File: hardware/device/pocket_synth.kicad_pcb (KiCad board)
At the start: 4 copper layers, 72 x 150 mm, 98 parts, among them J10 MIDI_OUT, J2 USB, J3 Micro_SD_Card_Det_Hirose_DM3AT, J6 LINE_IN, J8 LINE_OUT, J9 MIDI_IN, SW1 TRIG1, SW10 TRIG10, SW11 TRIG11, SW12 TRIG12, SW13 TRIG13, SW14 TRIG14, SW15 TRIG15, SW16 TRIG16, SW2 TRIG2, SW3 TRIG3, SW4 TRIG4, SW5 TRIG5, SW6 TRIG6, SW7 TRIG7, SW8 TRIG8, SW9 TRIG9, U1 VOL_PWR_POT, U10 TRIG9, U11 TRIG13, U12 TRIG10, U13 TRIG14, U14 TRIG11, U15 TRIG15, U16 TRIG12, U17 TRIG16, U18 STM32H743ZIT6, U2 TRIG1, U20 TPS62A02DRL, U21 TPS560200, U22 MAX17261xxTD, U23 BQ21040DBV, U25 TCA8418RTWR, U26 FUSB303BTMX, U27 FUSB302B01MPX, U3 TRIG2, U4 TRIG3, U5 TRIG4, U6 TRIG8, U7 TRIG7, U8 TRIG6, U9 TRIG5

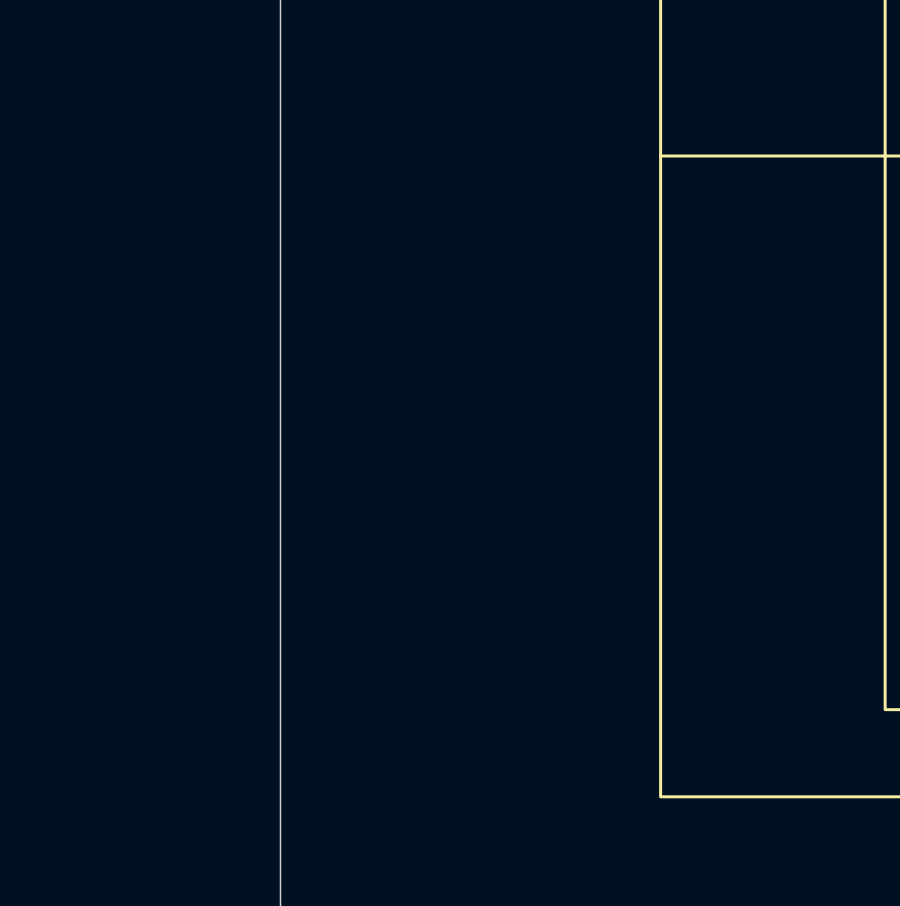
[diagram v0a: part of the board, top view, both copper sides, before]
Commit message: feat: project organization, add knob, pcb layout, and 3d models
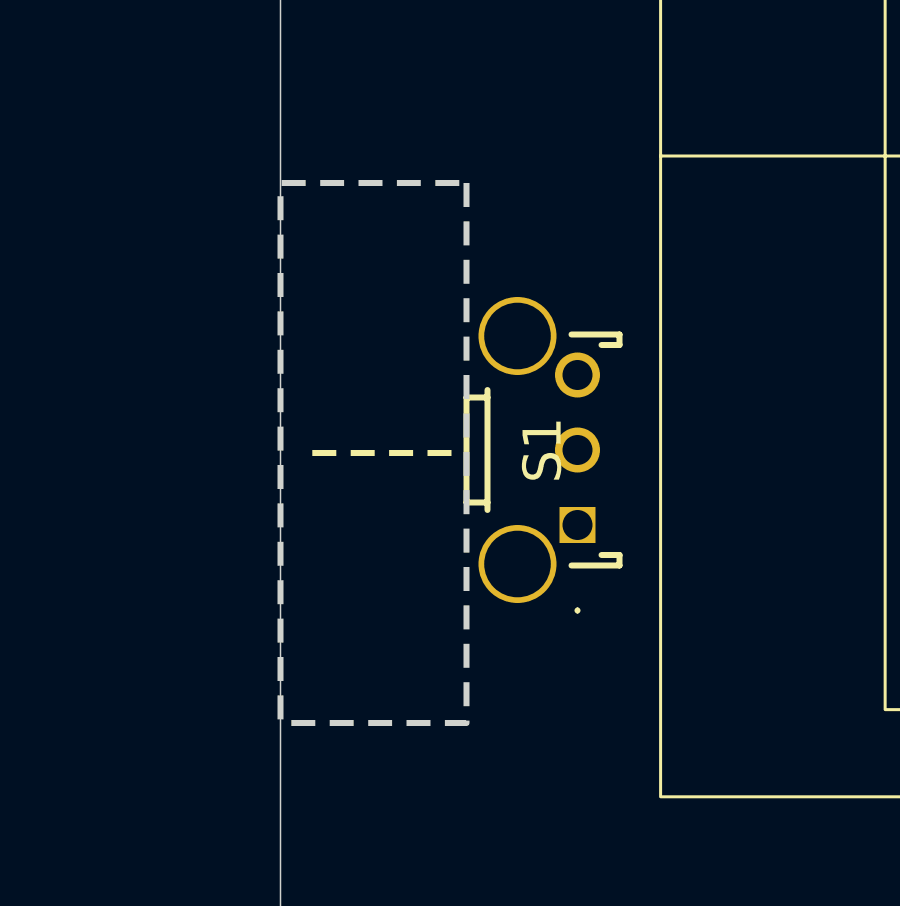
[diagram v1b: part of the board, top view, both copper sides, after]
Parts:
- added S1: ENCODER, pocket_synth:2416191-1, F.Cu at (46.7, 81.2)

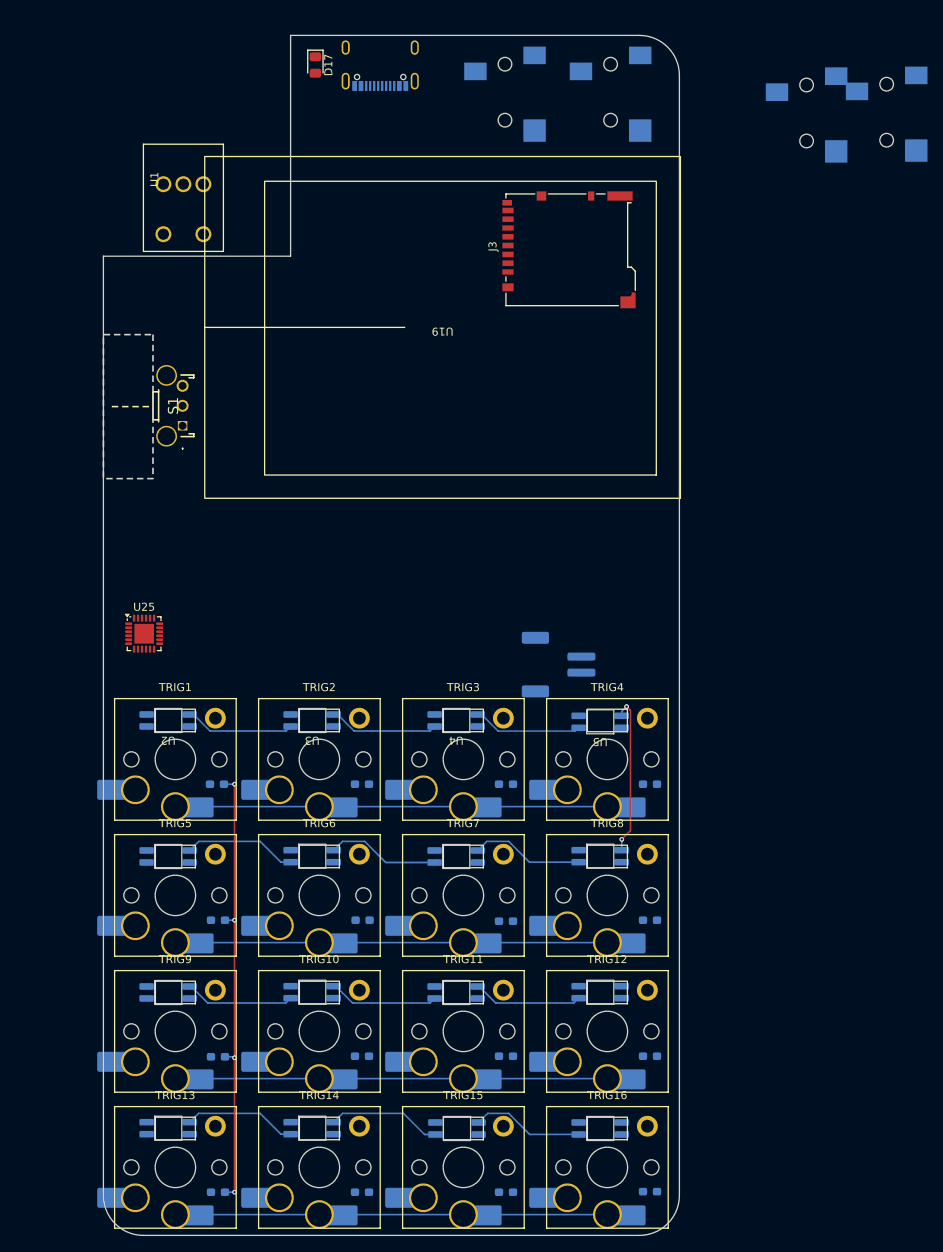
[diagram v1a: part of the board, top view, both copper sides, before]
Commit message: feat: various scroll wheel layout changes
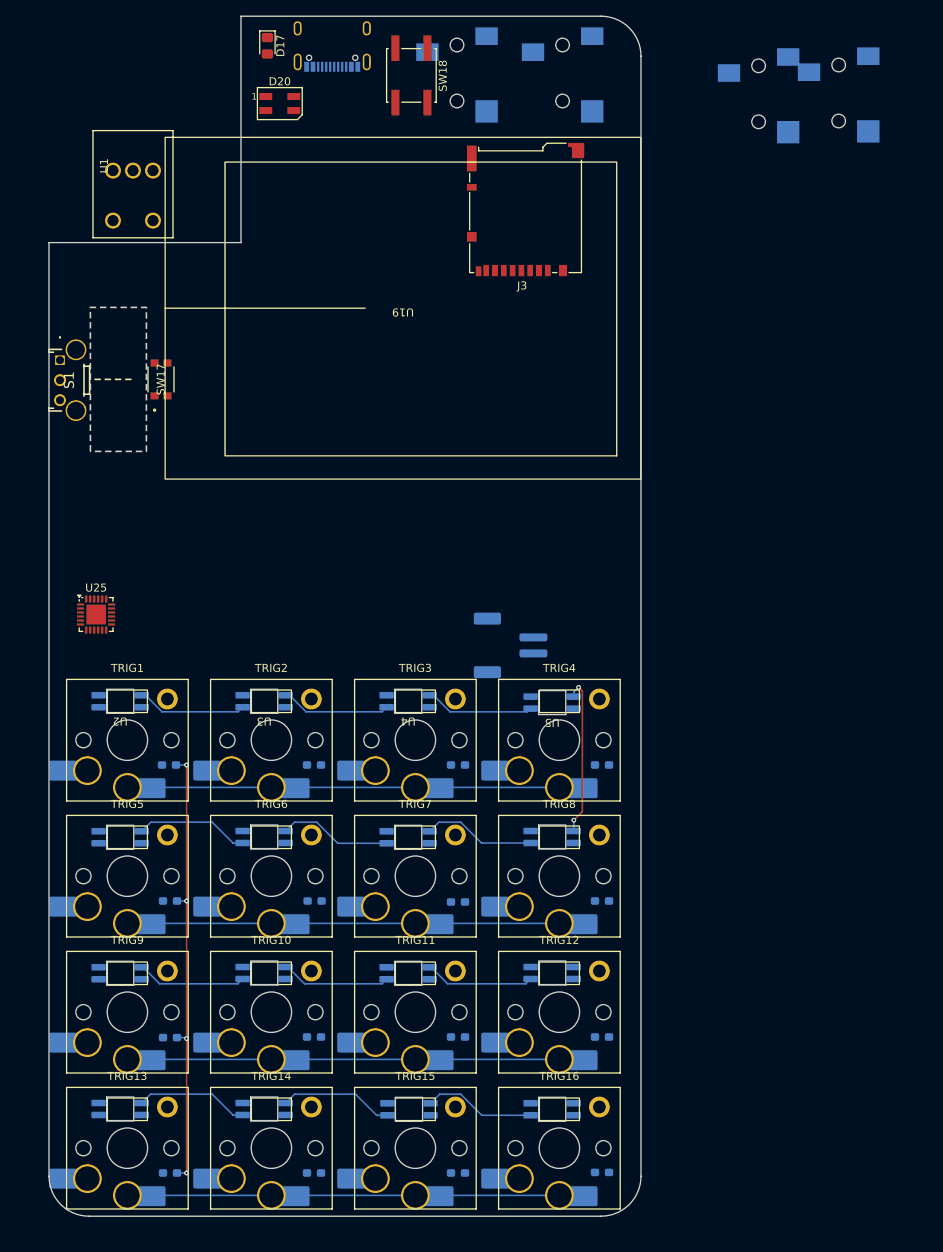
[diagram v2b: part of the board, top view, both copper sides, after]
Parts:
- added D20: METRONOME, LED_SMD:LED_SK6812MINI_PLCC4_3.5x3.5mm_P1.75mm, F.Cu at (58.9, 40.9)
- added SW17: KMR221NGLFS, pocket_synth:KMR221_CNK, F.Cu at (44.0, 75.4)
- added SW18: HELP, Button_Switch_SMD:SW_SPST_EVQQ2, F.Cu at (75.3, 37.4)
- moved S1 17.4 mm to (31.4, 73.0), turned to 90 degrees
- moved J3 7.41 mm to (89.6, 54.2), turned to 180 degrees
- moved U1 6.53 mm to (40.5, 49.3)
- moved D1 6.46 mm to (45.0, 123.6)
- moved D10 6.46 mm to (63.1, 157.6)
- moved D11 6.46 mm to (81.1, 157.6)
- moved D12 6.46 mm to (99.1, 157.6)
- moved D13 6.46 mm to (45.1, 174.6)
- moved D14 6.46 mm to (63.1, 174.6)
- moved D15 6.46 mm to (81.1, 174.6)
- moved D16 6.46 mm to (99.1, 174.5)
- moved D2 6.46 mm to (63.1, 123.6)
- moved D3 6.46 mm to (81.1, 123.6)
- moved D4 6.46 mm to (99.1, 123.6)
- moved D5 6.46 mm to (45.1, 140.6)
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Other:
- board size 72 x 150 mm -> 74 x 150 mm
- board text added: "Top or bottom row: SHIFT/FUNC EDIT YES/COMMIT NO/CANCEL NAV(igation) PLAY REC combine Yes/NO and PLAY/REC via shift/func key? would disallow combos with play/rec though.. play/rec as defaults and func changes to yes/no? NAV enables arrow key navigation and menus CALC/EXP mode that makes the keypad a calculator input (numbers and expressions)"
- board text removed: "Top or bottom row: SHIFT EDIT YES/COMMIT NO/CANCEL"

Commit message: feat: add various connectors
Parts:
- added J1: POT_CONN, pocket_synth:CONN_503480-0540_MOL, B.Cu at (56.7, 52.6)
- added J4: FX6-20P-0.8SV1(71), pocket_synth:FX6-20P-0.8SV1(71), B.Cu at (50.2, 75.5)
- moved L3 77.0 mm to (-86.6, 42.2)
- moved R56 77.0 mm to (-86.6, 49.7)
- moved TP14 77.0 mm to (-82.9, 44.0)
- moved C40 77.0 mm to (-90.9, 47.2)
- moved C41 77.0 mm to (-90.9, 49.7)
- moved C48 77.0 mm to (-70.7, 45.4)
- moved C50 77.0 mm to (-70.7, 51.4)
- moved L7 77.0 mm to (-86.6, 44.7)
- moved R29 77.0 mm to (-61.2, 46.0)
- moved R54 77.0 mm to (-61.2, 48.5)
- moved R55 77.0 mm to (-86.6, 47.2)
- moved R72 77.0 mm to (-86.6, 52.2)
- moved TP15 77.0 mm to (-82.9, 48.6)
- moved C39 77.0 mm to (-90.9, 44.7)
- moved C42 77.0 mm to (-90.9, 52.2)
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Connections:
- U1 pad 4: VDD -> unconnected-(U1-SW-Pad4)
- U1 pad 5: /Power/MCU_PWR_SW -> unconnected-(U1-SW-Pad5)
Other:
- board size 74 x 150 mm -> 74 x 138 mm

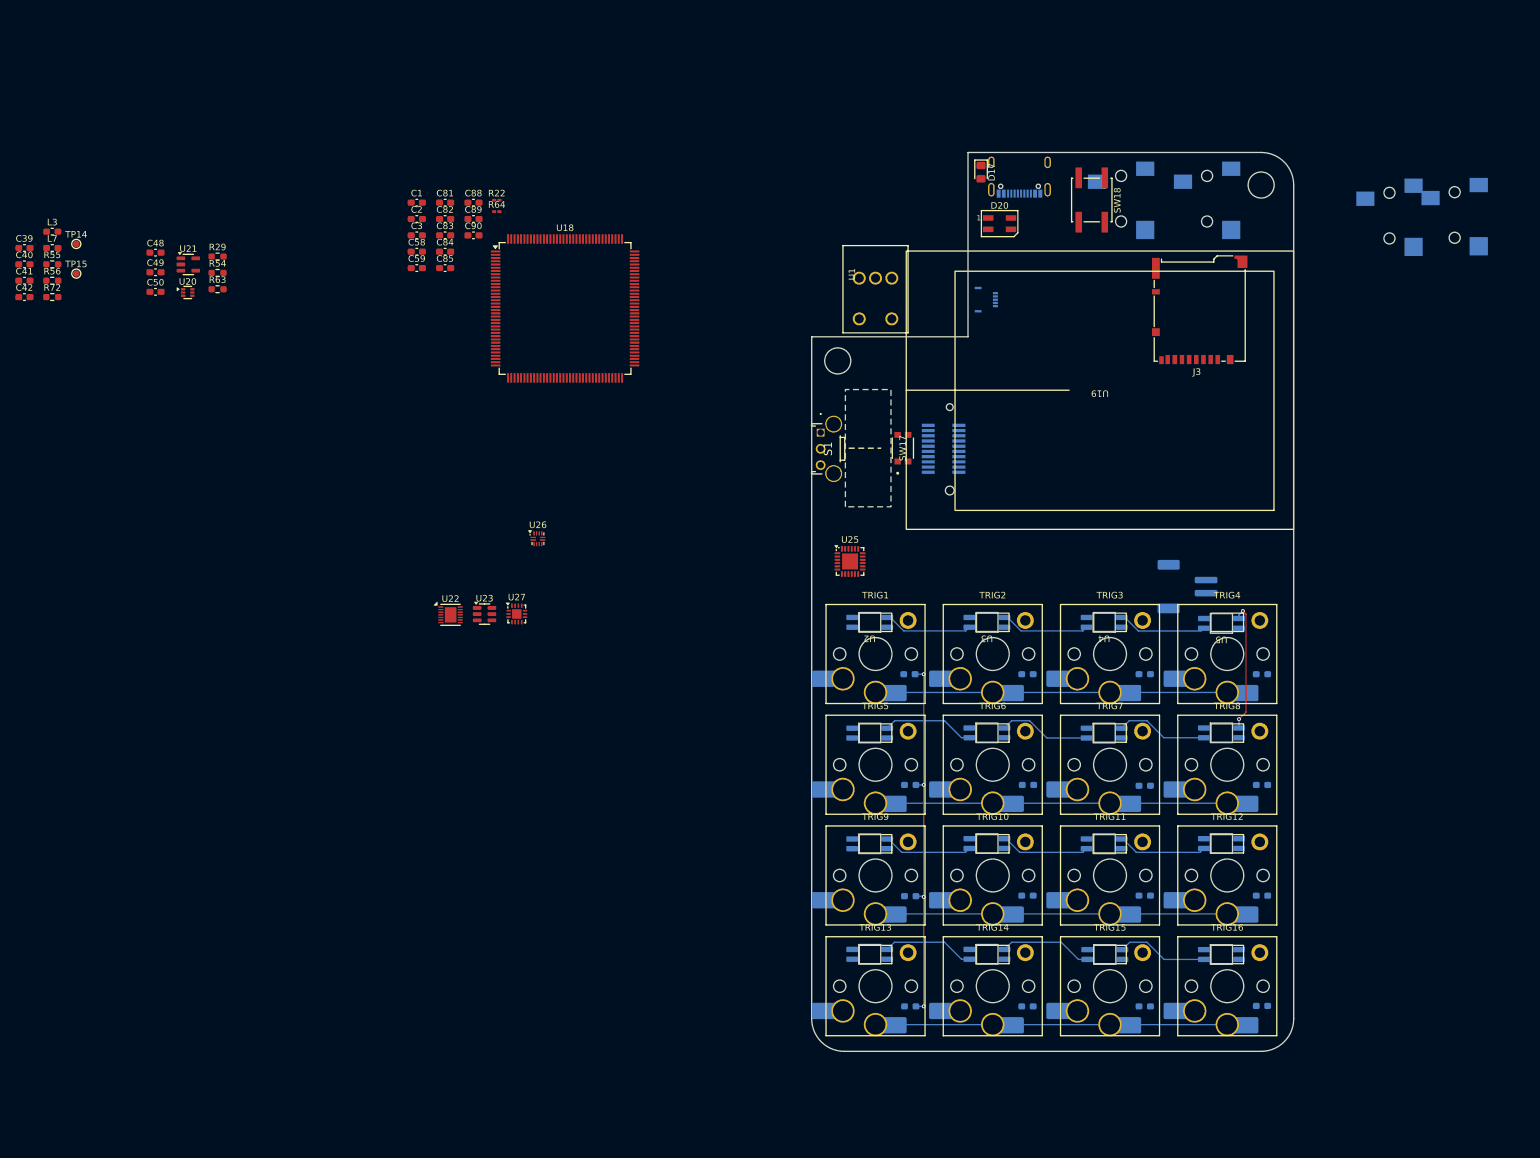
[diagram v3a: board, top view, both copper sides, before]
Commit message: feat: various footprint updates, 3d models, tollerances
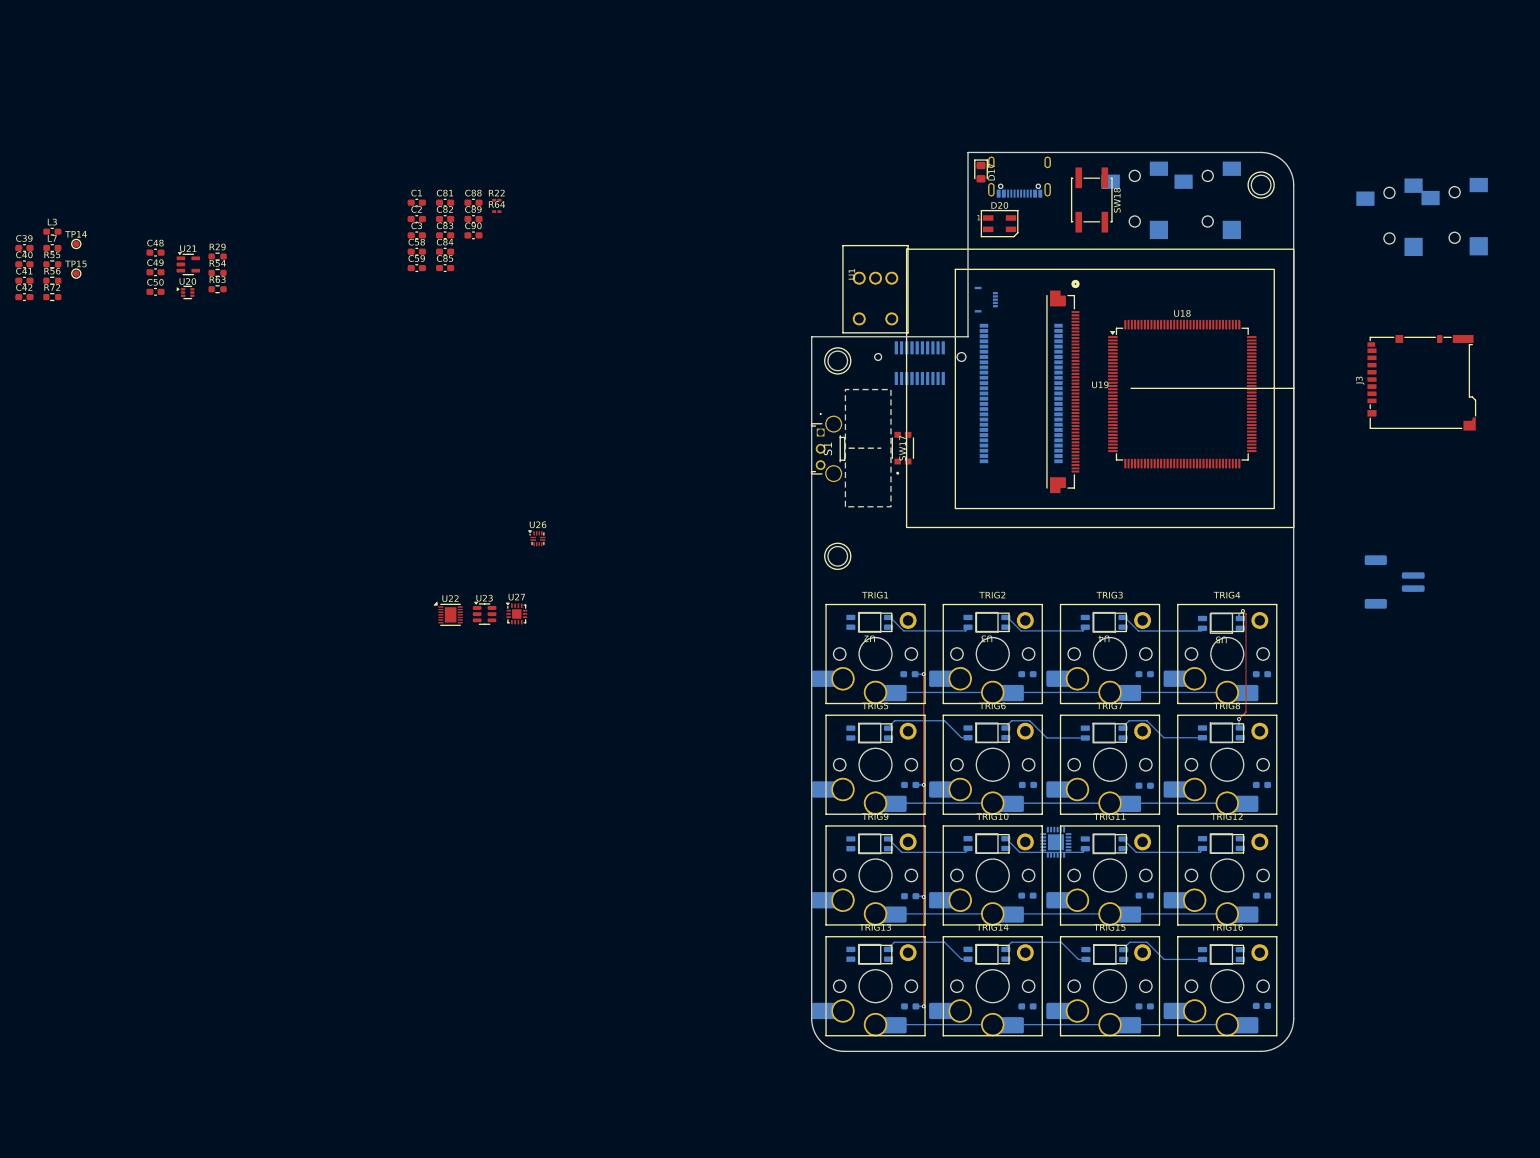
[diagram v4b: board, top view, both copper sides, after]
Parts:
- added IC1: IS42S16160J-7TLI, pocket_synth:SOP80P1176X120-54N, B.Cu at (62.2, 67.0)
- U19: value ~ -> ER-TFT024IPS-3
- U25: moved to B.Cu
- moved U18 95.7 mm to (86.9, 67.1)
- moved U25 53.5 mm to (67.5, 135.9), turned to 180 degrees
- moved J3 35.9 mm to (123.6, 65.4), turned to 90 degrees
- moved BT1 31.8 mm to (119.5, 96.0)
- moved J4 13.6 mm to (46.6, 62.4), turned to 0 degrees
- moved J8 2.10 mm to (79.6, 36.1)
- moved U19 0.29 mm to (74.3, 66.2), turned to 0 degrees
- moved J6 0.10 mm to (90.8, 36.1)
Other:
- outline, holes or cut-outs redrawn
